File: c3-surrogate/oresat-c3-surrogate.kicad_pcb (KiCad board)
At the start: 2 copper layers, 99.8 x 94.6 mm, 72 parts, among them J1 J-SAMTEC-TFM-120-X1-XXX-D-RA, J2 Conn_01x04, J4 Conn_01x02_Socket, Q1 PMV45EN, Q3 NTR2101P, Q4 NTR2101P, Q5 DMP3050LVT-7, SW2 Slide Switch, SW3 OS203011MV9QS1, SW4 EG1218, U1 MAX892LEUA+T, U2 LTC4412xS6, U4 LTC4412xS6, U5 TS5A21366, U6 Trinket-M0

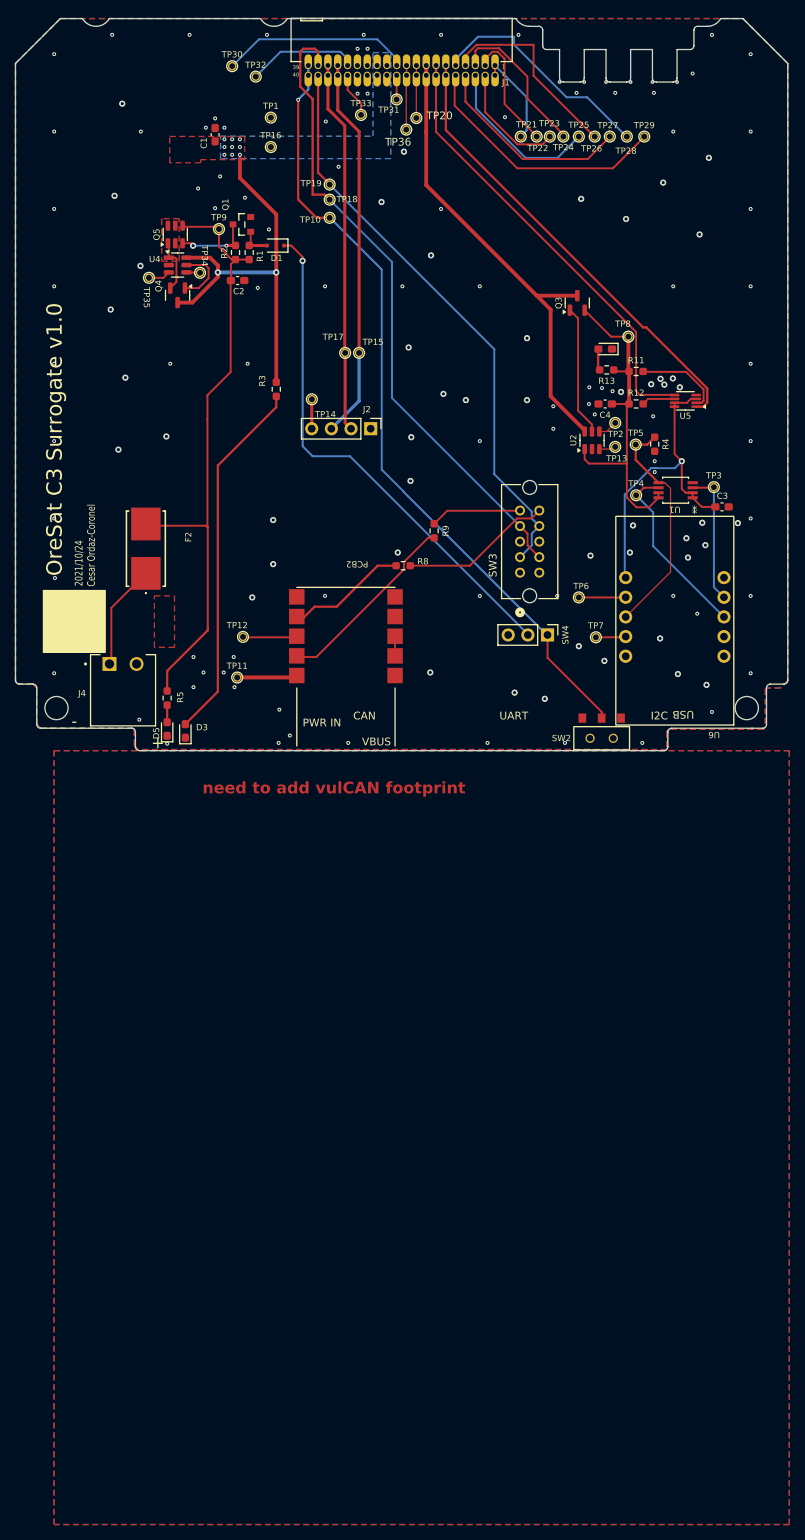
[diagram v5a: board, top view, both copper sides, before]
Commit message: Found one schematic error (no I2C connections), and lots of stupid unecessary polishing because OCD. Also updated symbol and library footprints.
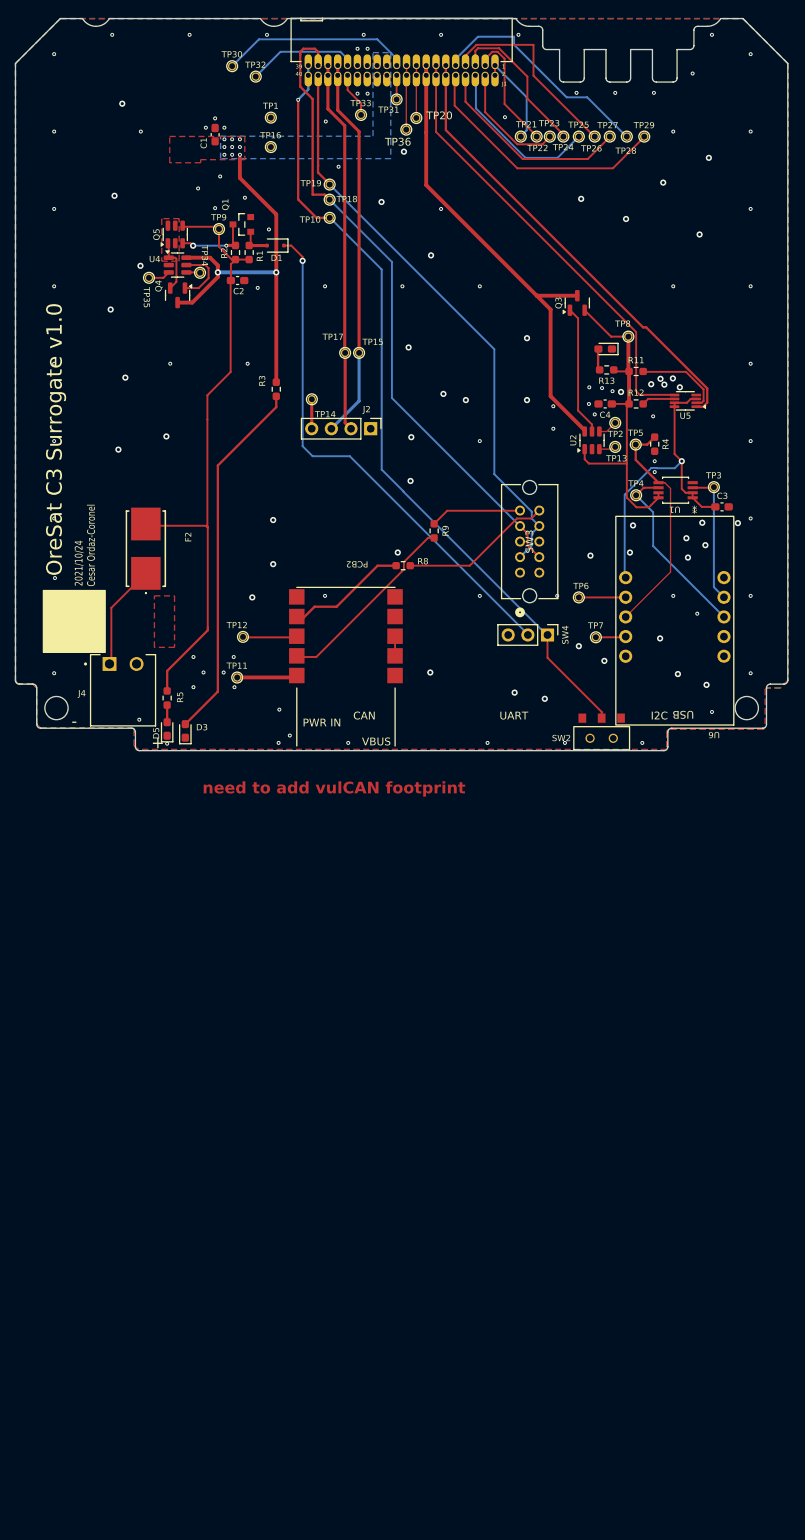
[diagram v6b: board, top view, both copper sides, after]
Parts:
- J1: footprint J-SAMTEC-TFM-120-X1-XXX-D-RA:J-SAMTEC-TFM-120-X1-XXX-D-RA -> oresat-connectors:J-SAMTEC-TFM-120-X1-XXX-D-RA
- PCB1: footprint oresat-cards:ORESAT-CARD-V1.3-GENERIC-3RF -> oresat-pcbs:ORESAT-CARD-V1.3-3RF
- Q3: value NTR2101P -> NTR4101P
- moved PCB1 70.5 mm to (149.9, 100.2)
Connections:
- net /~{SD} renamed ~{SD}
- R11 pad 2: Net-(U5-COM1) -> Net-(U5-COM2)
- R12 pad 2: Net-(U5-COM2) -> Net-(U5-COM1)
- TP6 pad 1: Net-(U6-SCL) -> Net-(U5-COM2)
- TP7 pad 1: Net-(U6-SDA) -> Net-(U5-COM1)
- U6 pad 7: Net-(U6-SCL) -> Net-(U5-COM2)
- U6 pad 9: Net-(U6-SDA) -> Net-(U5-COM1)
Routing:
- net Net-(U6-SCL): track 6.06 -> 0.00 mm
- net Net-(U5-COM2): track 4.32 -> 10.4 mm
- net Net-(U5-COM1): track 11.3 -> 15.2 mm
- net Net-(U6-SDA): track 3.89 -> 0.00 mm
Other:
- outline, holes or cut-outs redrawn
